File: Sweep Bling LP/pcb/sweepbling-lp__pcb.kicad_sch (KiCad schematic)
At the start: 46 parts, among them SW1 SW_Push, SW10 SW_Push, SW10_r1 SW_Push, SW11 SW_Push, SW11_r1 SW_Push, SW12 SW_Push, SW12_r1 SW_Push, SW13 SW_Push, SW13_r1 SW_Push, SW14 SW_Push, SW14_r1 SW_Push, SW15 SW_Push, SW15_r1 SW_Push, SW16 SW_Push, SW16_r1 SW_Push, SW17 SW_Push, SW17_r1 SW_Push, SW1_r1 SW_Push, SW2 SW_Push, SW2_r1 SW_Push, SW3 SW_Push, SW3_r1 SW_Push, SW4 SW_Push, SW4_r1 SW_Push, SW5 SW_Push, SW5_r1 SW_Push, SW6 SW_Push, SW6_r1 SW_Push, SW7 SW_Push, SW7_r1 SW_Push, SW8 SW_Push, SW8_r1 SW_Push, SW9 SW_Push, SW9_r1 SW_Push, U1 ProMicro-kbd, U2 ProMicro-kbd

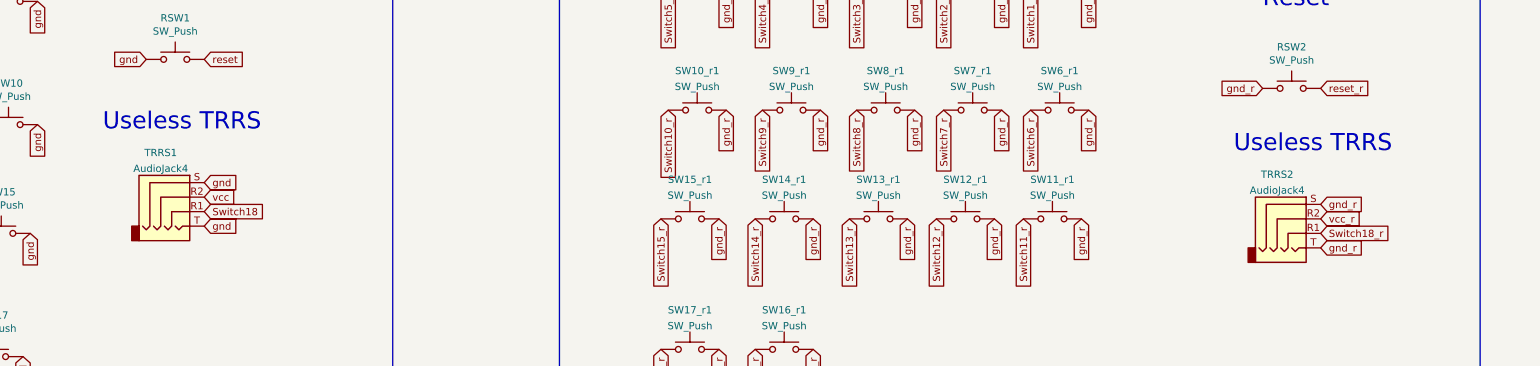
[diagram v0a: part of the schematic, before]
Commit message: remove trrs ports and connections
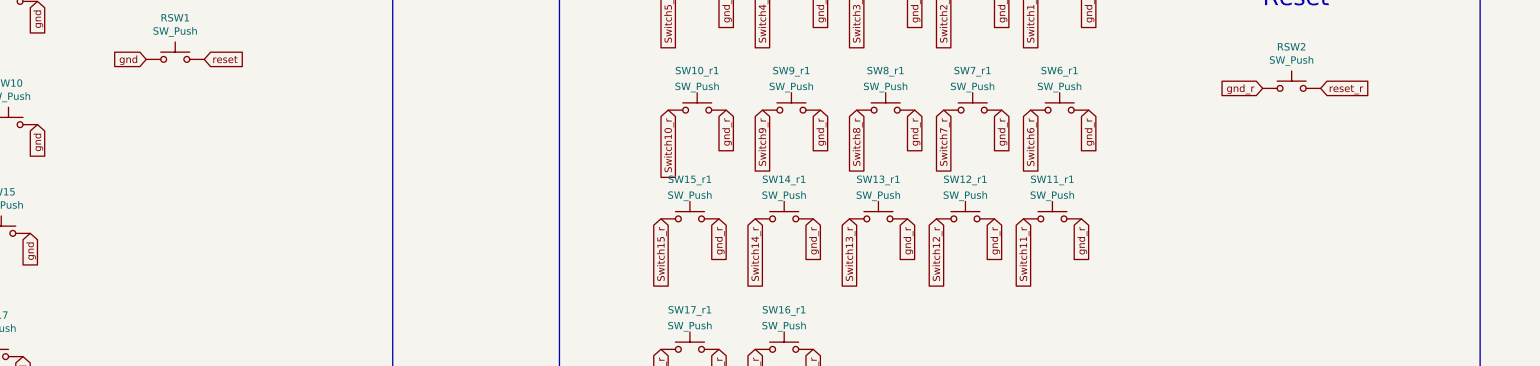
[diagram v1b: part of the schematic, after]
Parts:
- removed TRRS1, TRRS2: AudioJack4, symbol Connector:AudioJack4
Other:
- note removed: "Useless TRRS"
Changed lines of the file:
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@@
-    (effects (font (size 2.9972 2.9972)) (justify left bottom))
-  )
-  (text "Useless TRRS\n" (at 341.63 135.89 0)
     (effects (font (size 2.9972 2.9972)) (justify left bottom))
   )
@@
     (effects (font (size 2.9972 2.9972)) (justify left bottom))
   )
-  (text "Useless TRRS\n" (at 143.51 132.08 0)
-    (effects (font (size 2.9972 2.9972)) (justify left bottom))
-  )
   (text "Reset" (at 346.71 110.49 0)
     (effects (font (size 2.9972 2.9972)) (justify left bottom))
@@
     )
   )
-  (global_label "vcc" (shape input) (at 161.29 143.51 0) (fields_autoplaced)
-    (effects (font (size 1.27 1.27)) (justify left))
-    (property "Intersheet References" "${INTERSHEET_REFS}" (id 0) (at 34.29 73.66 0)
-      (effects (font (size 1.27 1.27)) hide)
-    )
-  )
   (global_label "gnd" (shape input) (at 82.55 149.86 270) (fields_autoplaced)
     (effects (font (size 1.27 1.27)) (justify right))
@@
     (property "Intersheet References" "${INTERSHEET_REFS}" (id 0) (at 316.1506 114.2052 90)
       (effects (font (size 1.27 1.27)) (justify right) hide)
-    )
-  )
-  (global_label "gnd_r" (shape input) (at 356.87 144.78 0) (fields_autoplaced)
-    (effects (font (size 1.27 1.27)) (justify left))
-    (property "Intersheet References" "${INTERSHEET_REFS}" (id 0) (at 364.3952 144.8594 0)
-      (effects (font (size 1.27 1.27)) (justify left) hide)
     )
   )
@@
     )
   )
-  (global_label "Switch18" (shape input) (at 161.29 146.05 0) (fields_autoplaced)
-    (effects (font (size 1.27 1.27)) (justify left))
-    (property "Intersheet References" "${INTERSHEET_REFS}" (id 0) (at 34.29 81.28 0)
-      (effects (font (size 1.27 1.27)) hide)
-    )
-  )
   (global_label "Switch11_r" (shape input) (at 254 62.23 180) (fields_autoplaced)
     (effects (font (size 1.27 1.27)) (justify right))
@@
     (effects (font (size 1.27 1.27)) (justify right))
     (property "Intersheet References" "${INTERSHEET_REFS}" (id 0) (at -104.14 13.97 0)
-      (effects (font (size 1.27 1.27)) hide)
-    )
-  )
-  (global_label "gnd" (shape input) (at 161.29 140.97 0) (fields_autoplaced)
-    (effects (font (size 1.27 1.27)) (justify left))
-    (property "Intersheet References" "${INTERSHEET_REFS}" (id 0) (at 34.29 73.66 0)
       (effects (font (size 1.27 1.27)) hide)
     )
@@
     )
   )
-  (global_label "Switch18_r" (shape input) (at 356.87 149.86 0) (fields_autoplaced)
-    (effects (font (size 1.27 1.27)) (justify left))
-    (property "Intersheet References" "${INTERSHEET_REFS}" (id 0) (at 228.6 -13.97 0)
-      (effects (font (size 1.27 1.27)) hide)
-    )
-  )
   (global_label "raw_r" (shape input) (at 342.9 48.26 270) (fields_autoplaced)
     (effects (font (size 1.27 1.27)) (justify right))
@@
     )
   )
-  (global_label "gnd" (shape input) (at 161.29 148.59 0) (fields_autoplaced)
-    (effects (font (size 1.27 1.27)) (justify left))
-    (property "Intersheet References" "${INTERSHEET_REFS}" (id 0) (at 34.29 81.28 0)
-      (effects (font (size 1.27 1.27)) hide)
-    )
-  )
   (global_label "Switch9_r" (shape input) (at 289.56 80.01 0) (fields_autoplaced)
     (effects (font (size 1.27 1.27)) (justify left))
@@
     )
   )
-  (global_label "gnd_r" (shape input) (at 356.87 152.4 0) (fields_autoplaced)
-    (effects (font (size 1.27 1.27)) (justify left))
-    (property "Intersheet References" "${INTERSHEET_REFS}" (id 0) (at 364.3952 152.4794 0)
-      (effects (font (size 1.27 1.27)) (justify left) hide)
-    )
-  )
   (global_label "Switch10" (shape input) (at 121.92 130.81 270) (fields_autoplaced)
     (effects (font (size 1.27 1.27)) (justify right))
@@
     (property "Intersheet References" "${INTERSHEET_REFS}" (id 0) (at 252.6506 114.2052 90)
       (effects (font (size 1.27 1.27)) (justify right) hide)
-    )
-  )
-  (global_label "vcc_r" (shape input) (at 356.87 147.32 0) (fields_autoplaced)
-    (effects (font (size 1.27 1.27)) (justify left))
-    (property "Intersheet References" "${INTERSHEET_REFS}" (id 0) (at 364.0928 147.2406 0)
-      (effects (font (size 1.27 1.27)) (justify left) hide)
     )
   )
@@
     (pin "1")
   )
-  (symbol (lib_id "Connector:AudioJack4") (at 351.79 147.32 0) (unit 1)
-    (in_bom yes) (on_board yes) (fields_autoplaced)
-    (property "Reference" "TRRS2" (id 0) (at 349.25 139.5435 0))
-    (property "Value" "AudioJack4" (id 1) (at 349.25 142.3186 0))
-    (property "Footprint" "" (id 2) (at 351.79 147.32 0)
-      (effects (font (size 1.27 1.27)) hide)
-    )
-    (property "Datasheet" "~" (id 3) (at 351.79 147.32 0)
-      (effects (font (size 1.27 1.27)) hide)
-    )
-    (pin "R1")
-    (pin "R2")
-    (pin "S")
-    (pin "T")
-  )
-  (symbol (lib_id "Connector:AudioJack4") (at 156.21 143.51 0) (unit 1)
-    (in_bom yes) (on_board yes) (fields_autoplaced)
-    (property "Reference" "TRRS1" (id 0) (at 153.67 135.7335 0))
-    (property "Value" "AudioJack4" (id 1) (at 153.67 138.5086 0))
-    (property "Footprint" "" (id 2) (at 156.21 143.51 0)
-      (effects (font (size 1.27 1.27)) hide)
-    )
-    (property "Datasheet" "~" (id 3) (at 156.21 143.51 0)
-      (effects (font (size 1.27 1.27)) hide)
-    )
-    (pin "R1")
-    (pin "R2")
-    (pin "S")
-    (pin "T")
-  )
   (sheet_instances
     (path "/" (page "1"))
@@
       (reference "SW_POWERR1") (unit 1) (value "SW_SPDT") (footprint "Kailh:SPDT_C128955")
     )
-    (path "/fb6a3ddb-b8c3-418d-b3fb-eef4cd8d34c3"
-      (reference "TRRS1") (unit 1) (value "AudioJack4") (footprint "")
-    )
-    (path "/2102dafa-b296-4185-917e-c329c2bd412b"
-      (reference "TRRS2") (unit 1) (value "AudioJack4") (footprint "")
-    )
     (path "/00000000-0000-0000-0000-00006049d3fb"

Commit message: re-set copper zones
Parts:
- removed RSW1, RSW2: SW_Push, kbd:ResetSW, symbol Switch:SW_Push
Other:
- note removed: "Reset"
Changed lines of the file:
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@@
-    (effects (font (size 2.9972 2.9972)) (justify left bottom))
-  )
-  (text "Reset" (at 151.13 105.41 0)
     (effects (font (size 2.9972 2.9972)) (justify left bottom))
   )
@@
     (effects (font (size 2.9972 2.9972)) (justify left bottom))
   )
-  (text "Reset" (at 346.71 110.49 0)
-    (effects (font (size 2.9972 2.9972)) (justify left bottom))
-  )
   (global_label "Switch14" (shape input) (at 54.61 69.85 180) (fields_autoplaced)
     (effects (font (size 1.27 1.27)) (justify right))
@@
     )
   )
-  (global_label "reset" (shape input) (at 161.29 119.38 0) (fields_autoplaced)
-    (effects (font (size 1.27 1.27)) (justify left))
-    (property "Intersheet References" "${INTERSHEET_REFS}" (id 0) (at 34.29 80.01 0)
-      (effects (font (size 1.27 1.27)) hide)
-    )
-  )
   (global_label "vcc" (shape input) (at 90.17 59.69 0) (fields_autoplaced)
     (effects (font (size 1.27 1.27)) (justify left))
@@
     (effects (font (size 1.27 1.27)) (justify right))
     (property "Intersheet References" "${INTERSHEET_REFS}" (id 0) (at 289.4806 159.9252 90)
-      (effects (font (size 1.27 1.27)) (justify right) hide)
-    )
-  )
-  (global_label "gnd" (shape input) (at 151.13 119.38 180) (fields_autoplaced)
-    (effects (font (size 1.27 1.27)) (justify right))
-    (property "Intersheet References" "${INTERSHEET_REFS}" (id 0) (at 34.29 80.01 0)
-      (effects (font (size 1.27 1.27)) hide)
-    )
-  )
-  (global_label "gnd_r" (shape input) (at 346.71 124.46 180) (fields_autoplaced)
-    (effects (font (size 1.27 1.27)) (justify right))
-    (property "Intersheet References" "${INTERSHEET_REFS}" (id 0) (at 339.1848 124.3806 0)
       (effects (font (size 1.27 1.27)) (justify right) hide)
     )
@@
     (effects (font (size 1.27 1.27)) (justify right))
     (property "Intersheet References" "${INTERSHEET_REFS}" (id 0) (at -104.14 16.51 0)
-      (effects (font (size 1.27 1.27)) hide)
-    )
-  )
-  (global_label "reset_r" (shape input) (at 356.87 124.46 0) (fields_autoplaced)
-    (effects (font (size 1.27 1.27)) (justify left))
-    (property "Intersheet References" "${INTERSHEET_REFS}" (id 0) (at 228.6 -13.97 0)
       (effects (font (size 1.27 1.27)) hide)
     )
@@
     (pin "2")
   )
-  (symbol (lib_id "Switch:SW_Push") (at 156.21 119.38 0) (unit 1)
-    (in_bom yes) (on_board yes)
-    (property "Reference" "RSW1" (id 0) (at 156.21 112.141 0))
-    (property "Value" "SW_Push" (id 1) (at 156.21 114.4524 0))
-    (property "Footprint" "kbd:ResetSW" (id 2) (at 156.21 114.3 0)
-      (effects (font (size 1.27 1.27)) hide)
-    )
-    (property "Datasheet" "~" (id 3) (at 156.21 114.3 0)
-      (effects (font (size 1.27 1.27)) hide)
-    )
-    (pin "1")
-    (pin "2")
-  )
   (symbol (lib_id "Switch:SW_SPDT") (at 142.24 48.26 0) (unit 1)
     (in_bom yes) (on_board yes)
@@
     (pin "9")
   )
-  (symbol (lib_id "Switch:SW_Push") (at 351.79 124.46 0) (unit 1)
-    (in_bom yes) (on_board yes)
-    (property "Reference" "RSW2" (id 0) (at 351.79 117.221 0))
-    (property "Value" "SW_Push" (id 1) (at 351.79 119.5324 0))
-    (property "Footprint" "kbd:ResetSW" (id 2) (at 351.79 119.38 0)
-      (effects (font (size 1.27 1.27)) hide)
-    )
-    (property "Datasheet" "~" (id 3) (at 351.79 119.38 0)
-      (effects (font (size 1.27 1.27)) hide)
-    )
-    (pin "1")
-    (pin "2")
-  )
   (symbol (lib_id "Switch:SW_SPDT") (at 337.82 45.72 0) (unit 1)
     (in_bom yes) (on_board yes)
@@
       (reference "BatGNDr1") (unit 1) (value "MountingHole_Pad") (footprint "kbd:1pin_conn")
     )
-    (path "/00000000-0000-0000-0000-0000604ea4f3"
-      (reference "RSW1") (unit 1) (value "SW_Push") (footprint "kbd:ResetSW")
-    )
-    (path "/00000000-0000-0000-0000-0000608f2176"
-      (reference "RSW2") (unit 1) (value "SW_Push") (footprint "kbd:ResetSW")
-    )
     (path "/00000000-0000-0000-0000-00006049e323"
